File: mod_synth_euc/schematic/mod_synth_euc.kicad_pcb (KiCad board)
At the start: 2 copper layers, 41.3 x 109.2 mm, 18 parts, among them J1 Clock In, J2 Conn_02x08_Odd_Even, J3 Gate Out

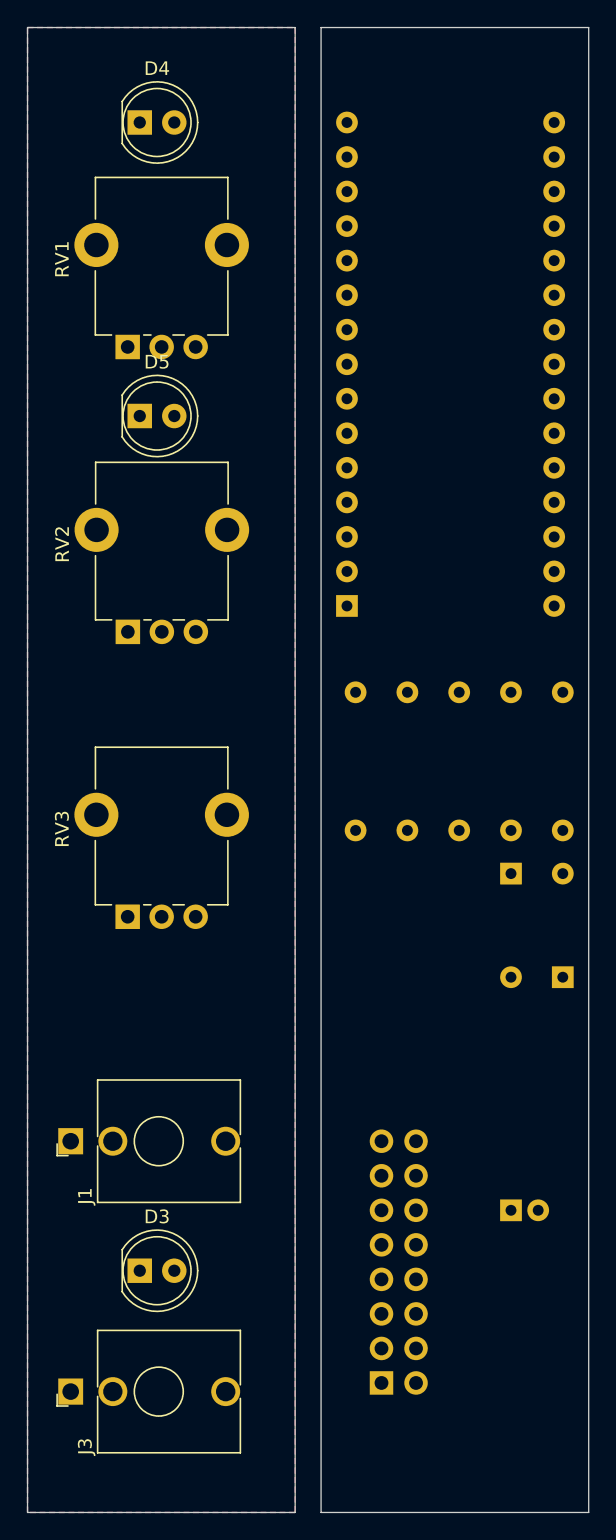
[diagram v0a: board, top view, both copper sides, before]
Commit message: Remove steps/pulses LEDs for one PCB
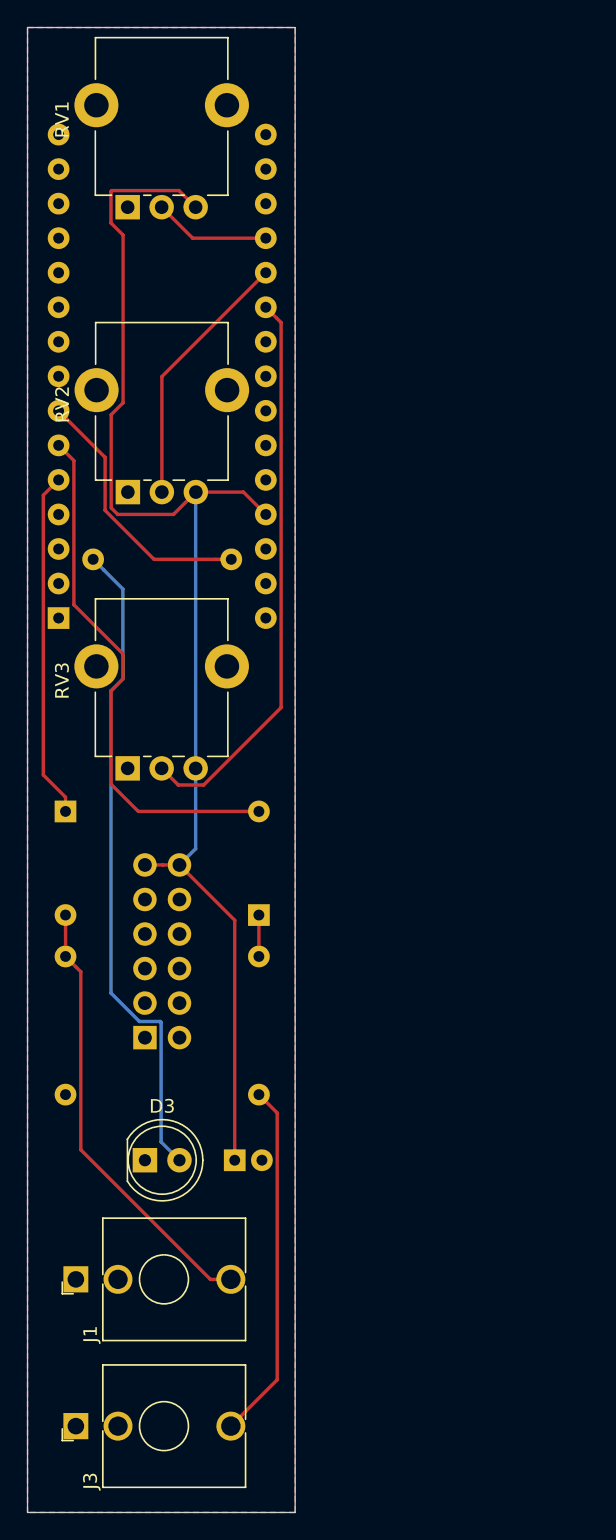
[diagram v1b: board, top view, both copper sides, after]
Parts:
- removed D4, D5: LED, LED_THT:LED_D5.0mm
- removed R4, R5: 220, Resistor_THT:R_Axial_DIN0207_L6.3mm_D2.5mm_P10.16mm_Horizontal
- J2: value Conn_02x08_Odd_Even -> Conn_02x06_Odd_Even; footprint Connector_IDC:IDC-Header_2x08_P2.54mm_Vertical -> Connector_IDC:IDC-Header_2x06_P2.54mm_Vertical
- moved D1 38.6 mm to (40.9, 89.4), turned to 270 degrees
- moved R1 37.7 mm to (40.9, 100.1), turned to 270 degrees
- moved J2 30.8 mm to (46.7, 106.0)
- moved R3 27.8 mm to (42.9, 70.9), turned to 0 degrees
- moved R2 26.9 mm to (55.1, 110.2)
- moved A1 21.2 mm to (40.4, 75.2)
- moved C1 20.7 mm to (53.3, 115.1)
- moved D2 18.8 mm to (55.1, 97.0), turned to 90 degrees
- moved RV3 10.9 mm to (45.5, 86.2)
- moved RV2 10.3 mm to (45.5, 65.9)
- moved RV1 10.3 mm to (45.5, 45.0)
- moved J1 10.2 mm to (41.7, 123.8)
- moved D3 8.14 mm to (46.7, 115.1)
- moved J3 2.57 mm to (41.7, 134.6)
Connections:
- A1 pad 8: /led_steps -> Net-(A1-Pad8)
- A1 pad 9: /led_pulses -> Net-(A1-Pad9)
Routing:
- net +5V: track 0.00 -> 97.6 mm
- net Net-(D3-Pad2): track 0.00 -> 48.4 mm
- net /shift: track 0.00 -> 41.6 mm
- net /gate: track 0.00 -> 38.9 mm
- net Net-(D1-Pad2): track 0.00 -> 32.7 mm
- net Net-(J3-PadT): track 0.00 -> 26.4 mm
- net /clock: track 0.00 -> 25.5 mm
- net /led_gate: track 0.00 -> 19.5 mm
- net /pulses: track 0.00 -> 19.3 mm
- net /steps: track 0.00 -> 8.60 mm
- net Net-(D2-Pad1): track 0.00 -> 3.05 mm
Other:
- board size 41.3 x 109.2 mm -> 19.7 x 109.2 mm

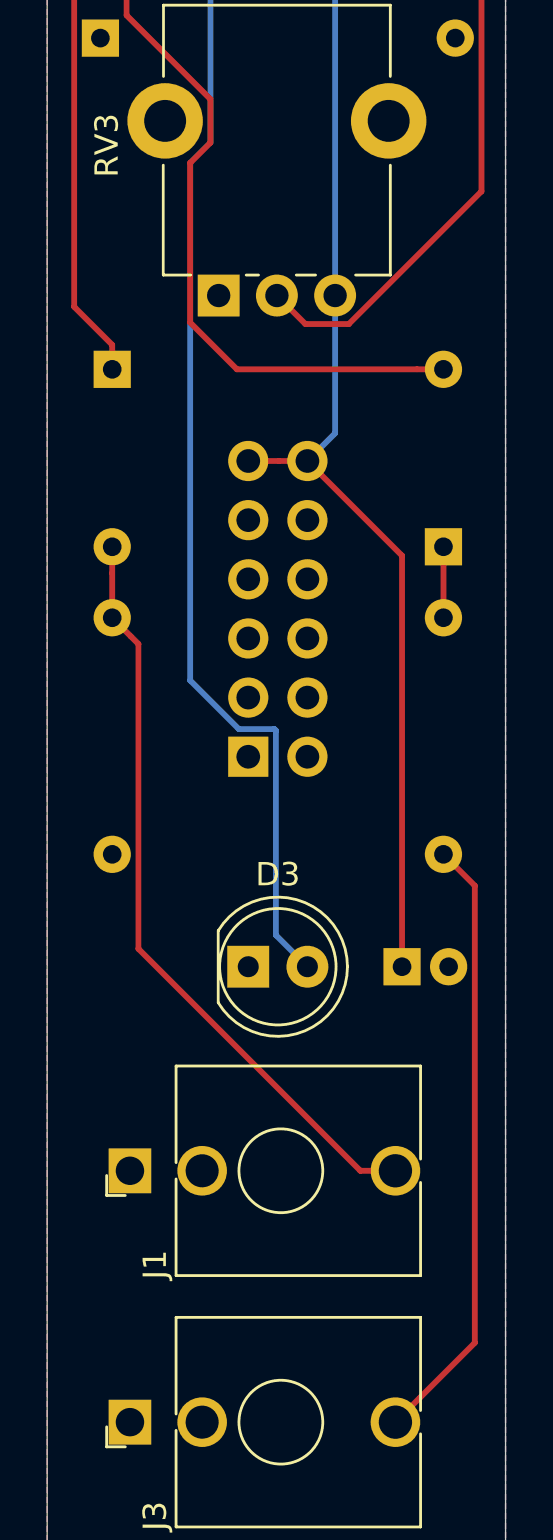
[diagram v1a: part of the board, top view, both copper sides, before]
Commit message: Update ignore values, change connector on euclid
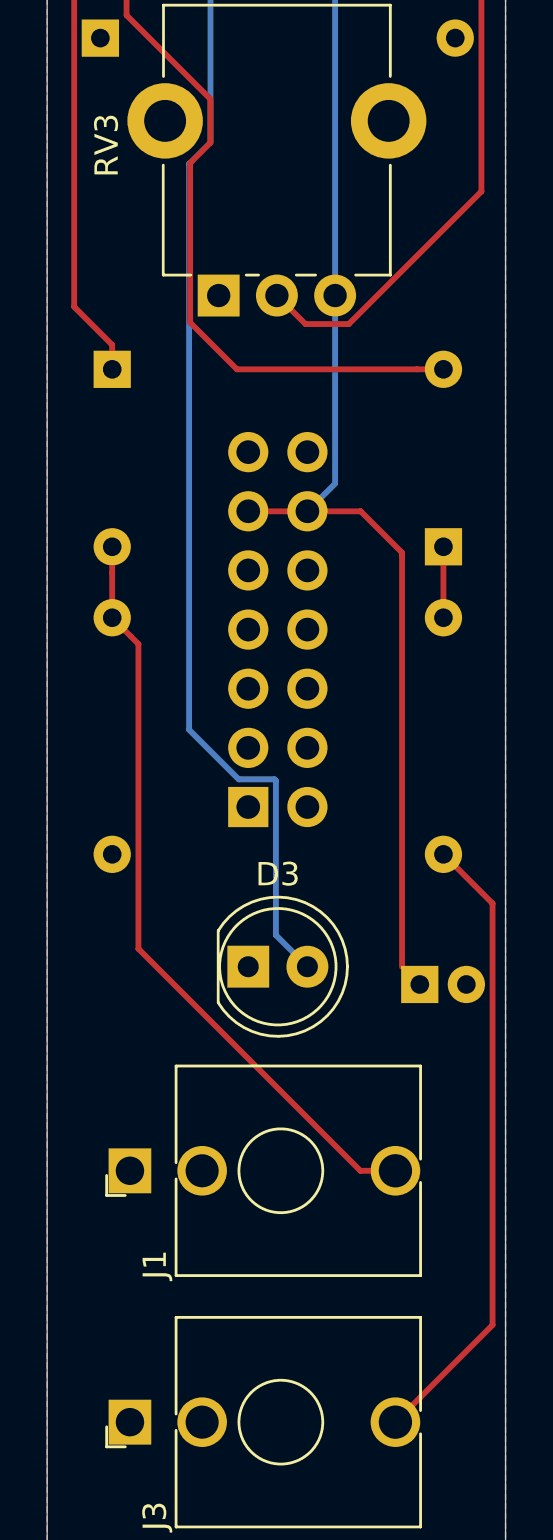
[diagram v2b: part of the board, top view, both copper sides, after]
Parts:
- J2: value Conn_02x06_Odd_Even -> Conn_02x07_Odd_Even; footprint Connector_IDC:IDC-Header_2x06_P2.54mm_Vertical -> Connector_IDC:IDC-Header_2x07_P2.54mm_Vertical
- moved J2 2.16 mm to (46.7, 108.2)
- moved C1 1.08 mm to (54.1, 115.8)
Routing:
- net +5V: track 97.6 -> 98.9 mm
- net Net-(J3-PadT): track 26.4 -> 27.0 mm
